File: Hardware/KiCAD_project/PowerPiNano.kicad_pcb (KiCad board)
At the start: 2 copper layers, 53 x 53 mm, 67 parts, among them J1 SW_interface, J2 USB_B_Mini, J3 resistor network 1, J4 IOs, J5 IOs, J6 resistor network 2, Q1 MMBT3904, Q2 MMBT3904, Q3 MMBT3904, Q4 MMBT3904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

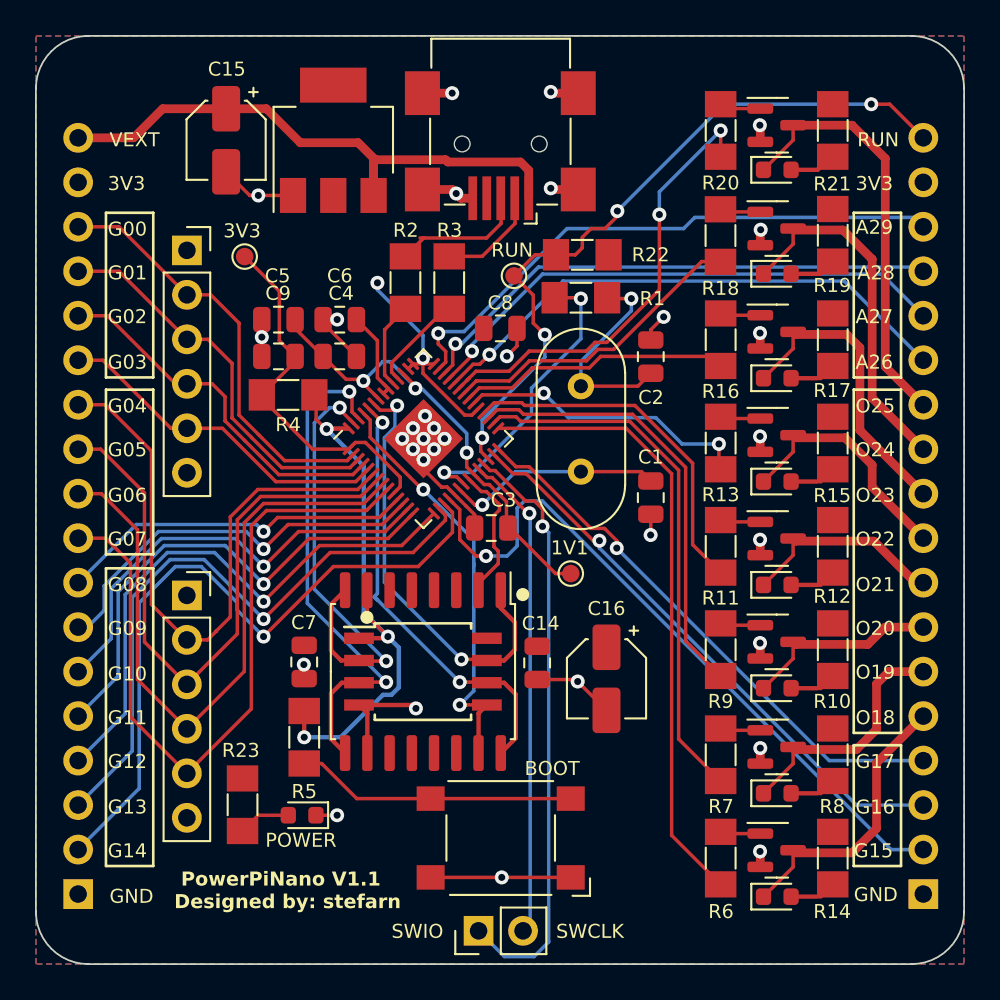
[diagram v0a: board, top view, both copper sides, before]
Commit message: replaced schematic symbols of the electrolytic caps for the correct ones
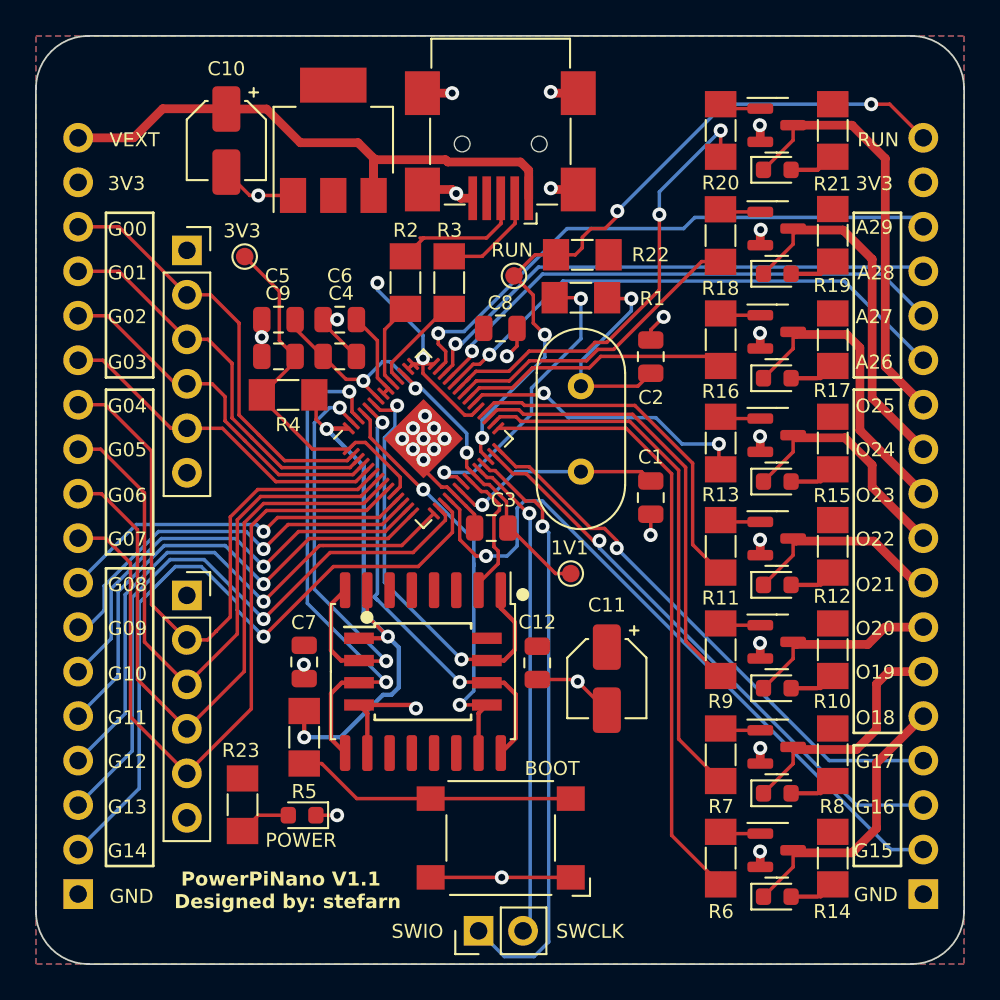
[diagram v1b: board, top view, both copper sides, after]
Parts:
- removed C14: 100nF, Capacitor_SMD:C_0805_2012Metric
- removed C15, C16: 10µF, Capacitor_SMD:CP_Elec_4x3
- added C10: 10µF, Capacitor_SMD:CP_Elec_4x3, F.Cu at (132.9, 85.0)
- added C11: 10µF, Capacitor_SMD:CP_Elec_4x3, F.Cu at (154.6, 115.7)
- added C12: 100nF, Capacitor_SMD:C_0805_2012Metric, F.Cu at (150.6, 114.8)
- C1, C2: value 47pF -> 56pF
